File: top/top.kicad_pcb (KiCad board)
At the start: 2 copper layers, 28.8 x 40.6 mm, 24 parts, among them P1 CONN_10, P2 CONN_5, U1 IQS572, U4 ESD

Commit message: Add via pattern.
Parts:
- moved P1 42.7 mm to (196.2, 156.7), turned to 180 degrees
- moved U1 39.7 mm to (205.7, 150.3)
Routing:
- net (no net): track 0.00 -> 151.2 mm, vias 0 -> 48
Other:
- net class Default: via_dia 0.889 -> 0.7112; via_drill 0.635 -> 0.381
- rule via_min_drill: 0.508 -> 0.381
- rule via_min_size: 0.889 -> 0.7112

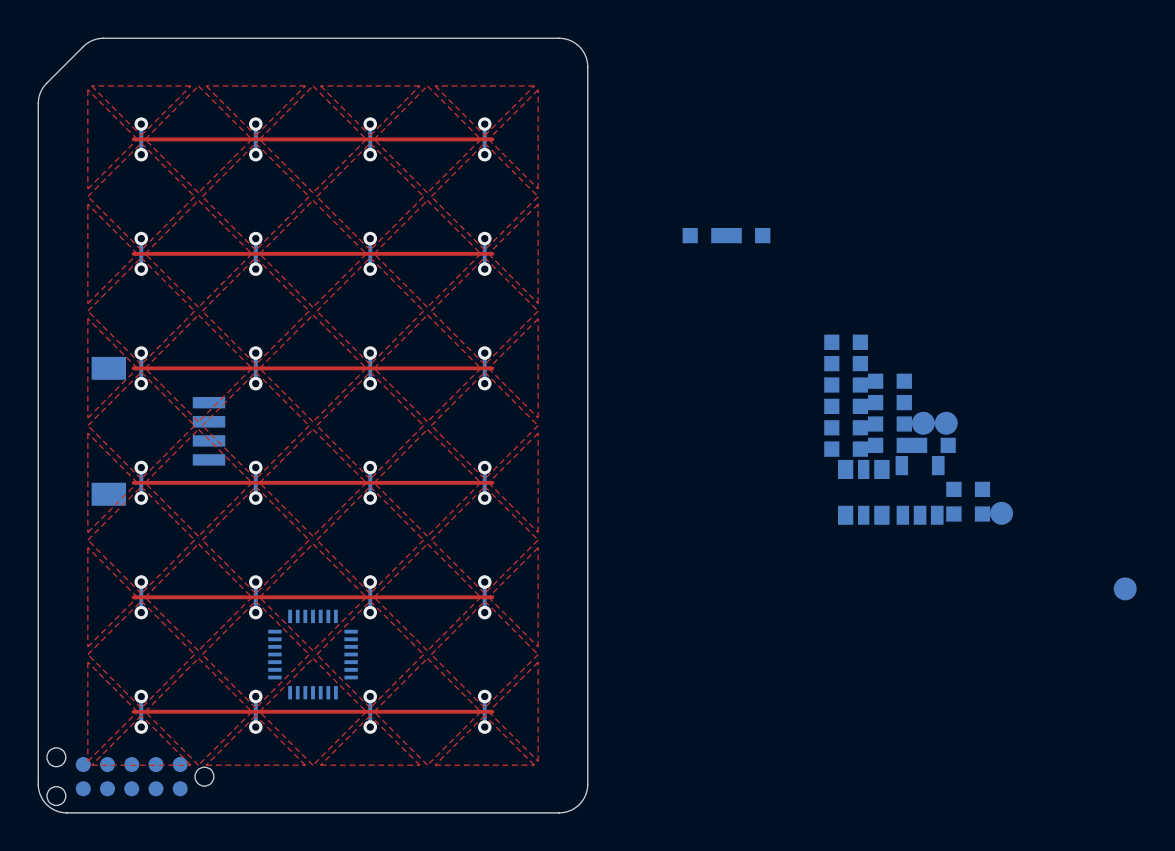
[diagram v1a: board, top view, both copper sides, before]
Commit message: Change touchpad sensor footprint. GND ring added to PCB.
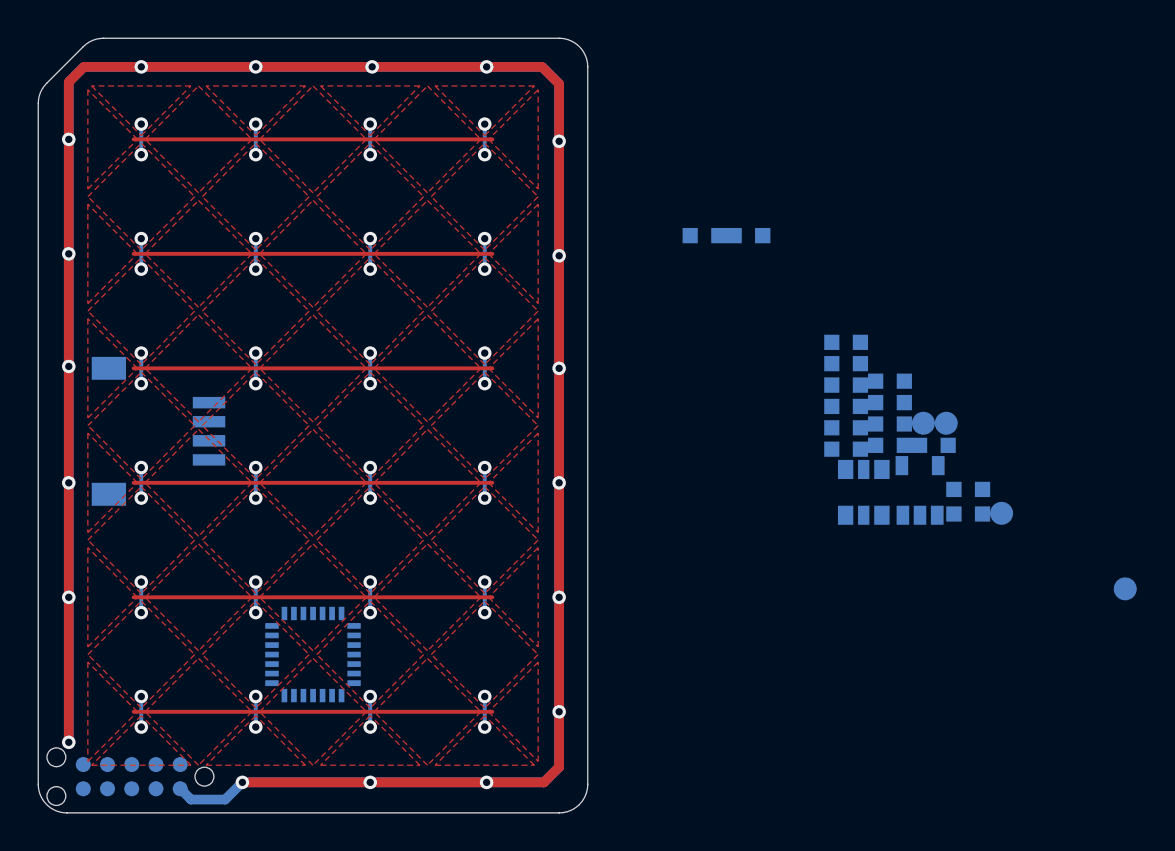
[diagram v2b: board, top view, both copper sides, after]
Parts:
- U1: footprint ugl:QFN-28_4x4_Pitch0.4mm -> ugl:QFN-28_4.3x4.3_Pitch0.5mm
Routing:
- net GND: track 0.00 -> 231.4 mm, vias 0 -> 19

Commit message: End of day commit. (Unrouted pattern.)
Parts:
- removed C13: 0.1uF, ugl:SM0603
- TP_GND1: value TEST_POINT -> GND
- TP_POUT1: value TEST_POINT -> POUT
- TP_RDY1: value TEST_POINT -> RDY
- TP_TOUT1: value TEST_POINT -> TOUT
- moved TP_TOUT1 39.2 mm to (201.2, 148.8)
- moved TP_POUT1 38.8 mm to (201.2, 151.4)
- moved TP_RDY1 38.8 mm to (209.6, 149.8)
- moved R7 34.6 mm to (203.7, 141.3), turned to 90 degrees
- moved R6 34.4 mm to (205.6, 141.3), turned to 90 degrees
- moved R2 34.1 mm to (202.5, 144.0)
- moved C4 33.6 mm to (206.6, 146.5), turned to 270 degrees
- moved TP_GND1 33.2 mm to (211.7, 157.0)
- moved C5 31.2 mm to (205.8, 143.9), turned to 270 degrees
- moved R1 30.1 mm to (204.5, 143.9), turned to 270 degrees
- moved U4 29.5 mm to (205.3, 137.9)
- moved C3 28.9 mm to (207.9, 146.5), turned to 270 degrees
- moved C6 26.9 mm to (207.1, 143.9), turned to 270 degrees
- moved VR1 26.9 mm to (210.7, 143.3), turned to 180 degrees
- moved C7 26.0 mm to (207.6, 135.5), turned to 270 degrees
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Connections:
- P1 pad 2: +5V -> Net-(P1-Pad2)
- P2 pad 2: /SCL_BOTTOM -> /SDA_BOTTOM
- P2 pad 3: /SDA_BOTTOM -> /SCL_BOTTOM
- R6 pad 1: /SDA -> /SCL
- R6 pad 2: /SDA_BOTTOM -> /SCL_BOTTOM
- R7 pad 1: /SCL -> /SDA
- R7 pad 2: /SCL_BOTTOM -> /SDA_BOTTOM
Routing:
- net GND: track 231.4 -> 285.8 mm
- net /NRST: track 0.00 -> 23.0 mm
- net /RDY: track 0.00 -> 20.8 mm
- net +3V3: track 0.00 -> 11.9 mm
- net /PGM: track 0.00 -> 10.6 mm
- net /SCL: track 0.00 -> 10.5 mm
- net /SDA: track 0.00 -> 9.61 mm
- net +5V: track 0.00 -> 8.64 mm
- net /SCL_BOTTOM: track 0.00 -> 8.48 mm
- net /VCC_BOTTOM: track 0.00 -> 8.36 mm
- net /SDA_BOTTOM: track 0.00 -> 5.61 mm
- net Net-(TP_POUT1-Pad1): track 0.00 -> 3.57 mm
- net Net-(C3-Pad2): track 0.00 -> 3.19 mm
- net Net-(TP_TOUT1-Pad1): track 0.00 -> 3.12 mm

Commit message: First final version of PCB and SCH.
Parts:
- P1: value CONN_10 -> CONN_6; footprint ugl:Tag_Connect_2x5_Header_With_No_Legs -> ugl:Tag_Connect_2x3_Header_No_Legs
- U1: footprint ugl:QFN-28_4.3x4.3_Pitch0.5mm -> ugl:QFN-28_4.3x4.3_Pitch0.5mm_Alt_PAD
- moved TP_RDY1 2.06 mm to (210.9, 148.2)
- moved TP_POUT1 1.86 mm to (199.7, 150.3)
- moved C1 1.30 mm to (209.8, 146.5)
- moved TP_TOUT1 1.10 mm to (201.2, 147.7)
- moved P1 0.81 mm to (195.4, 156.6)
- moved R2 0.61 mm to (202.6, 144.6)
- moved R7 0.60 mm to (204.3, 141.3)
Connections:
- P1 pad 1: GND -> /NRST
- P1 pad 2: Net-(P1-Pad2) -> /PGM
- P1 pad 3: /SCL -> GND
- P1 pad 4: /SDA -> +3V3
- P1 pad 5: Net-(P1-Pad5) -> /SCL
- P1 pad 6: Net-(P1-Pad6) -> /SDA
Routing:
- net (no net): track 151.2 -> 0.00 mm, vias 48 -> 0
- net /RX0: track 0.00 -> 37.0 mm, vias 0 -> 1
- net /RX1: track 0.00 -> 31.5 mm, vias 0 -> 1
- net /SCL: track 10.5 -> 38.7 mm
- net /RX2: track 0.00 -> 25.9 mm, vias 0 -> 1
- net /RX3: track 0.00 -> 20.5 mm, vias 0 -> 1
- net /TX0: track 0.00 -> 18.5 mm, vias 0 -> 13
- net /TX3: track 0.00 -> 18.0 mm, vias 0 -> 13
- net /SDA: track 9.61 -> 27.5 mm
- net /RDY: track 20.8 -> 3.65 mm
- net +3V3: track 11.9 -> 28.1 mm
- net /RX4: track 0.00 -> 15.2 mm, vias 0 -> 1
- net /TX1: track 0.00 -> 14.5 mm, vias 0 -> 12
- net /TX2: track 0.00 -> 12.1 mm, vias 0 -> 13
- net GND: track 285.8 -> 296.9 mm
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- added copper zone on F.Cu, net /RX0
- added copper zone on F.Cu, net /RX1
- added copper zone on F.Cu, net /RX2
- added copper zone on F.Cu, net /RX3
- added copper zone on F.Cu, net /RX4
- added copper zone on F.Cu, net /RX5
- added copper zone on F.Cu, net /TX0
- added copper zone on F.Cu, net /TX1
- added copper zone on F.Cu, net /TX2
- added copper zone on F.Cu, net /TX3
- added copper zone on B.Cu, net GND
- removed copper zone on F.Cu, net (none)
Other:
- net class Default: clearance 0.2032 -> 0.1778
- rule trace_clearance: 0.2032 -> 0.1778
- board text added: "84981-4"

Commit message: Change tag connector 2x3 to 2x5.
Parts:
- P1: value CONN_6 -> CONN_10; footprint ugl:Tag_Connect_2x3_Header_No_Legs -> ugl:Tag_Connect_2x5_Header_With_No_Legs_Parallel_Numbering
- moved P1 1.00 mm to (196.4, 156.6)
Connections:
- net /RX6 renamed Net-(U1-Pad16)
- net /RX7 renamed Net-(U1-Pad17)
- net /TX4 renamed Net-(U1-Pad22)
- net /TX5 renamed Net-(U1-Pad23)
- net /TX6 renamed Net-(U1-Pad24)
- net /TX7 renamed Net-(U1-Pad25)
- net /TX8 renamed Net-(U1-Pad26)
- P1 pad 1: /NRST -> Net-(P1-Pad1)
- P1 pad 2: /PGM -> Net-(P1-Pad2)
- P1 pad 3: GND -> Net-(P1-Pad3)
- P1 pad 4: +3V3 -> Net-(P1-Pad4)
- P1 pad 5: /SCL -> GND
- P1 pad 6: /SDA -> /PGM
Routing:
- net /NRST: track 18.9 -> 21.7 mm, vias 0 -> 2
- net GND: track 296.9 -> 294.5 mm
- net /TX3: track 18.0 -> 19.1 mm

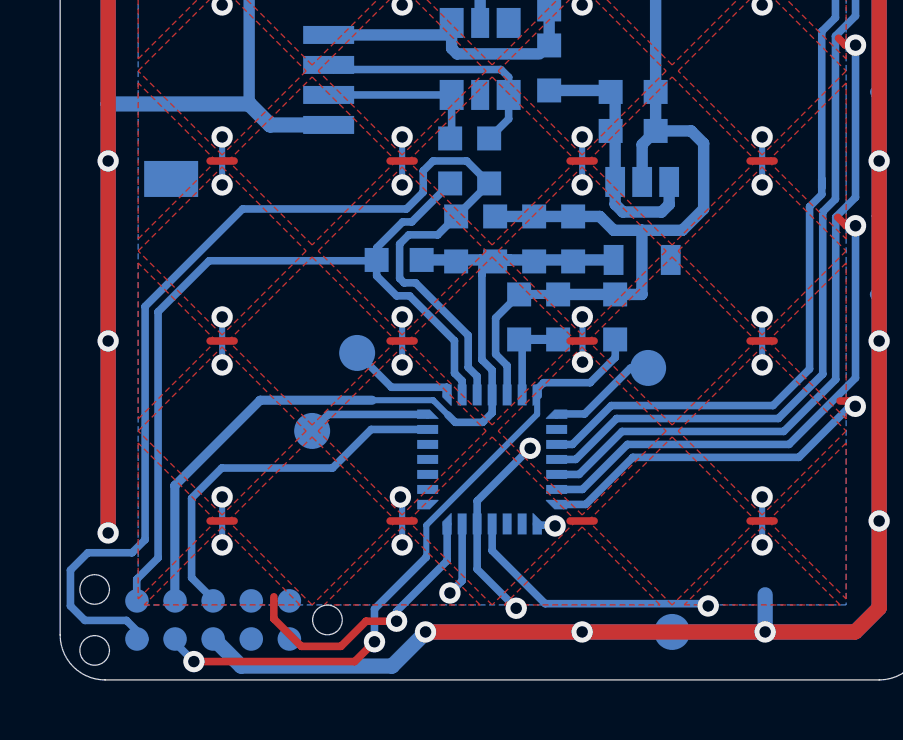
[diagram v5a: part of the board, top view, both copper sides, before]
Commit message: Change UPA header pinout.
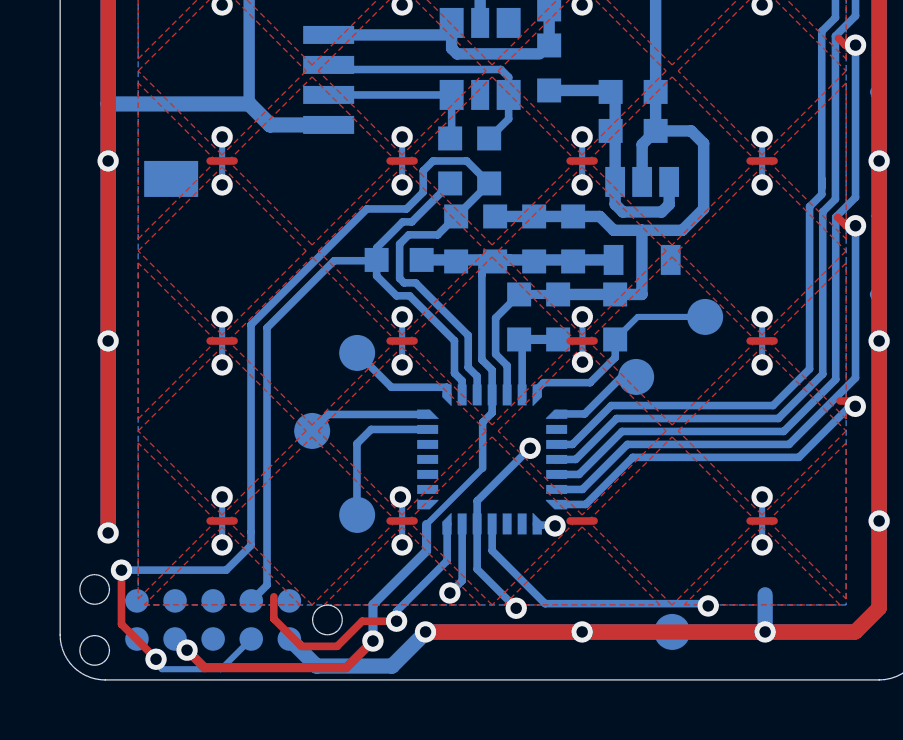
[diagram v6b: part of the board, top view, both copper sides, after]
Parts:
- added TP_NRST1: NRST, ugl:Test_Point, B.Cu at (212.8, 146.5)
- added TP_PGM1: PGM, ugl:Test_Point, B.Cu at (201.2, 153.1)
- moved TP_RDY1 0.50 mm to (210.5, 148.5)
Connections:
- P1 pad 1: Net-(P1-Pad1) -> GND
- P1 pad 10: /SDA -> Net-(P1-Pad10)
- P1 pad 3: Net-(P1-Pad3) -> /SCL
- P1 pad 4: Net-(P1-Pad4) -> /SDA
- P1 pad 5: GND -> Net-(P1-Pad5)
- P1 pad 6: /PGM -> Net-(P1-Pad6)
- P1 pad 7: /NRST -> +3V3
- P1 pad 8: +3V3 -> Net-(P1-Pad8)
- P1 pad 9: /SCL -> Net-(P1-Pad9)
- U1 pad 27: /PGM -> Net-(TP_PGM1-Pad1)
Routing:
- net /NRST: track 21.7 -> 7.15 mm, vias 2 -> 0
- net /PGM: track 12.5 -> 0.00 mm
- net Net-(TP_PGM1-Pad1): track 0.00 -> 4.93 mm
- net /SDA: track 27.6 -> 23.6 mm
- net GND: track 294.5 -> 292.0 mm
- net /SCL: track 39.2 -> 40.5 mm, vias 0 -> 2
- net +3V3: track 28.2 -> 28.9 mm, vias 0 -> 2
- net /RDY: track 3.65 -> 3.15 mm

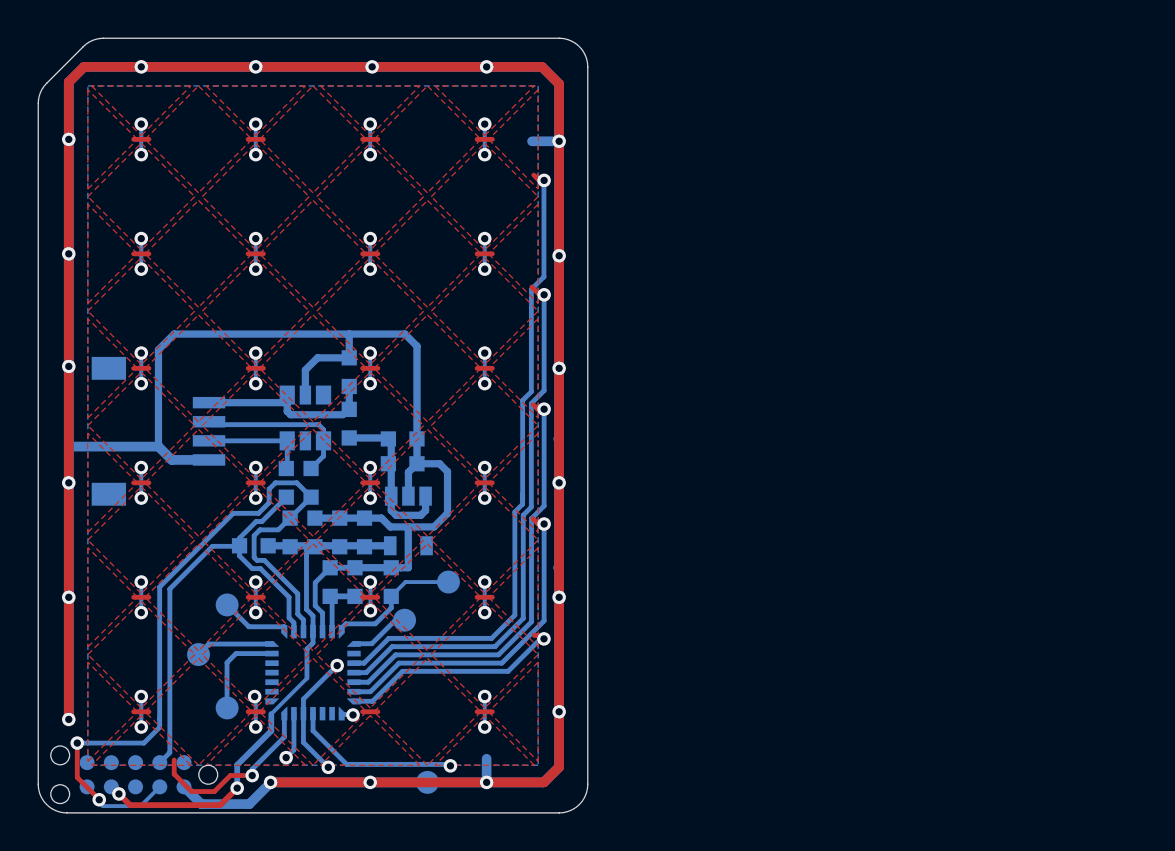
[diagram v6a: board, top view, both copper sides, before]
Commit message: Use +5V instead of +3V3 on programmer connector.
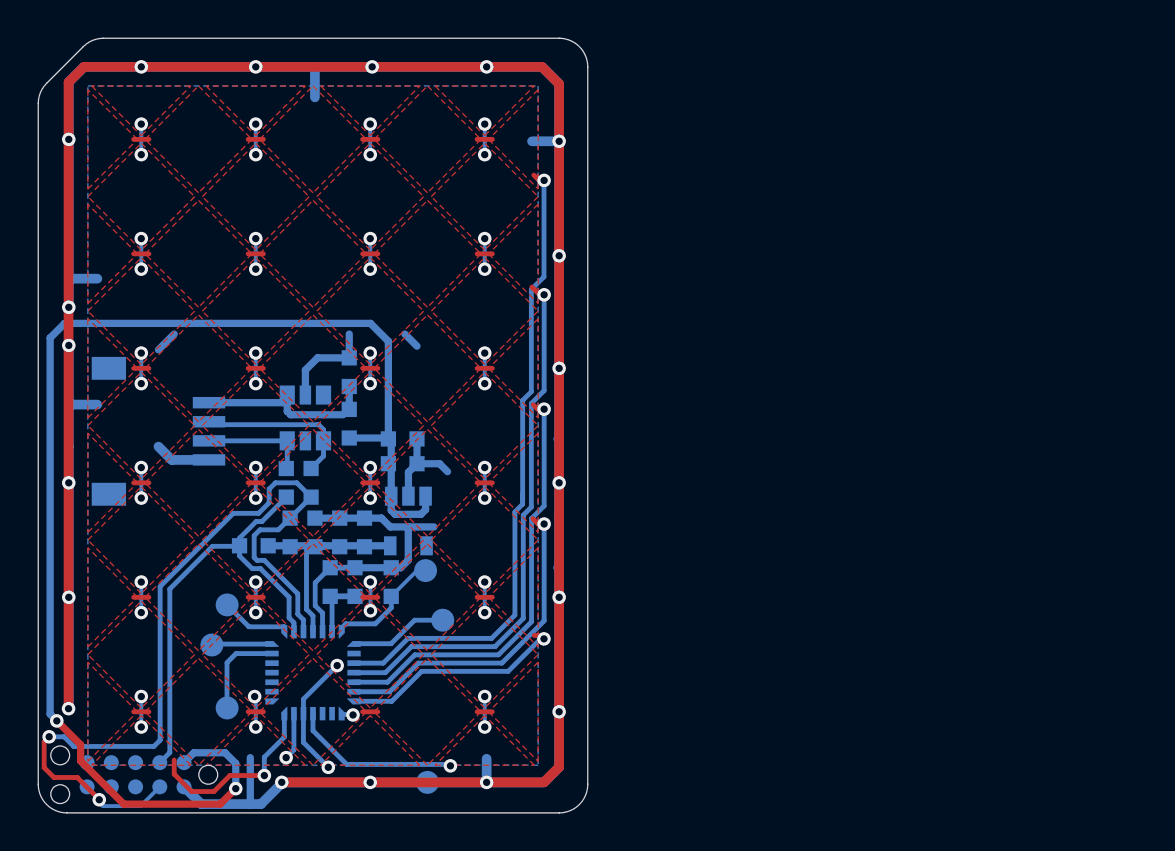
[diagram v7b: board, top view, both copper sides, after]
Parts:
- moved TP_RDY1 2.00 mm to (212.5, 148.5)
- moved TP_NRST1 1.34 mm to (211.6, 145.9)
- moved TP_POUT1 0.86 mm to (200.4, 149.8)
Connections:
- P1 pad 2: Net-(P1-Pad2) -> +5V
- P1 pad 7: +3V3 -> Net-(P1-Pad7)
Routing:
- net +5V: track 8.64 -> 68.8 mm, vias 0 -> 2
- net GND: track 292.0 -> 265.2 mm
- net +3V3: track 28.9 -> 11.6 mm, vias 2 -> 0
- net /SCL: track 40.5 -> 44.5 mm
- net /RDY: track 3.15 -> 5.14 mm
- net /NRST: track 7.15 -> 6.20 mm
- net Net-(TP_POUT1-Pad1): track 4.08 -> 3.31 mm
